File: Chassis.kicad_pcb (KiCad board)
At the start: 4 copper layers, 80 x 80.1 mm, 75 parts, among them IC1 LV2862YDDCR, IC2 RT6285GSP, J1 FR_JST, J10 IN_XT30, J11 SWD_IN, J12 Conn_01x08_Pin, J13 GIM1_JST, J14 GIM2_JST, J15 GIM1_XT30, J16 GIM2_XT30, J17 SWD_OUT, J18 CHA_XT30, J19 SHOO_XT30, J2 BR_JST, J20 GIM_XT30, J21 OUT_JST, J22 5V_XT30, J23 UART_IN, J24 UART_Out, J25 REF_IN, J26 REF_OUT, J27 CAN2_IN, J28 CAN2_OUT, J3 FL_JST, J4 BL_JST, J5 FR_XT30, J6 BR_XT30, J7 FL_XT30, J8 BL_XT30, J9 IN_JST

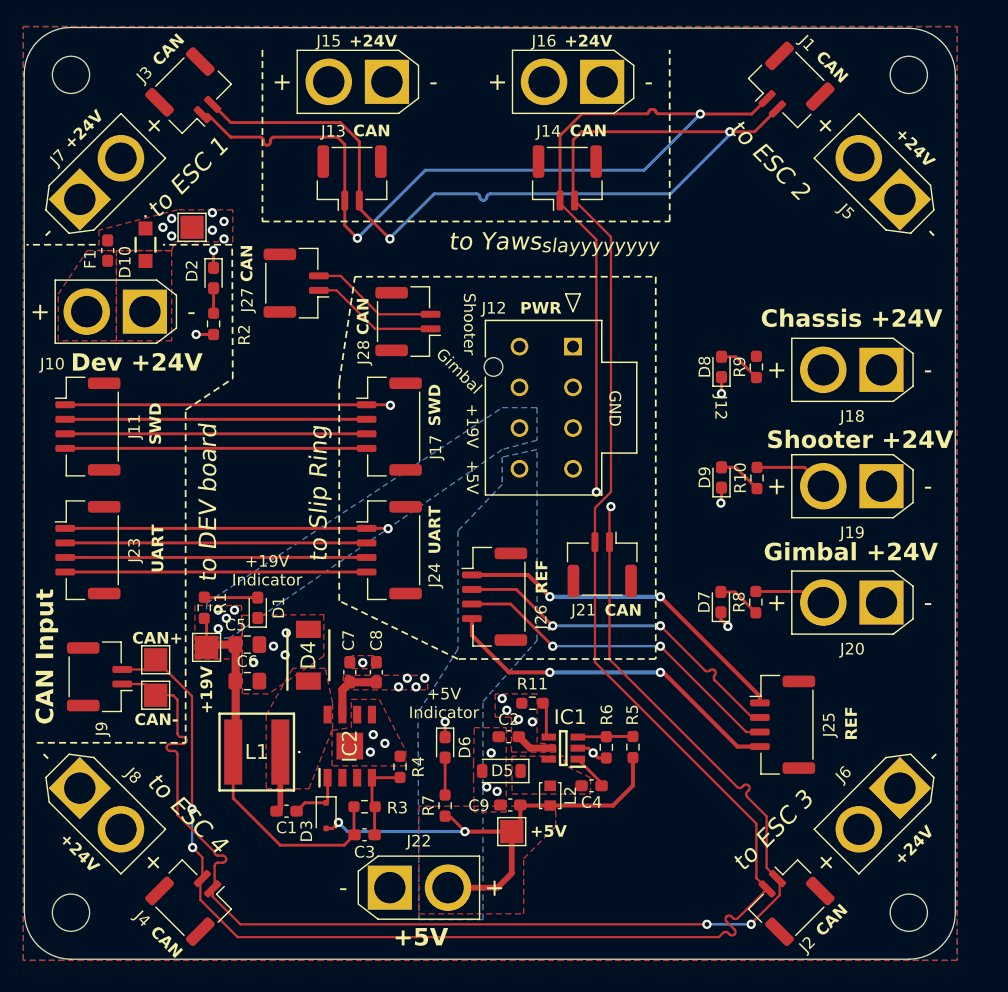
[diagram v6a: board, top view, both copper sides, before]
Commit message: Replace inductor with larger
Idk how much current it'll need + invalid inductor data for spreadsheet
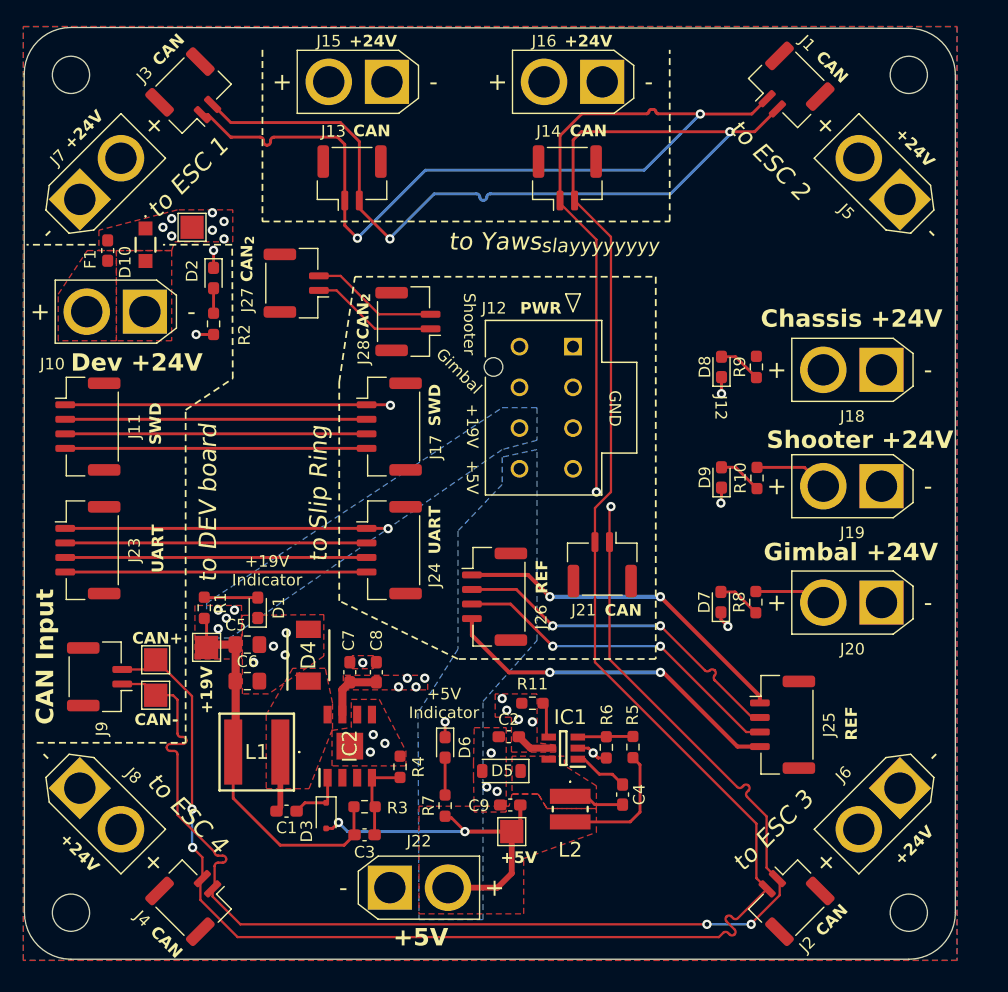
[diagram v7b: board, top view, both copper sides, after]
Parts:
- L2: footprint Inductor_SMD:L_Murata_LQH2MCNxxxx02_2.0x1.6mm -> Robomaster_Passives:SRN3012BTA330M
- moved C4 2.77 mm to (99.8, 91.2), turned to -90 degrees
- moved L2 2.07 mm to (95.2, 92.5)
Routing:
- net /24V -> 19V Buck Convertor/SW_{5}: track 0.00 -> 4.80 mm
- net /24V -> 19V Buck Convertor/BOOT_{5}: track 2.89 -> 4.75 mm
- net +5V: track 42.6 -> 41.1 mm
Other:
- board text added: "CAN_{2}"

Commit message: Update and generate IBOM
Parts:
- C2: value 2.2 μF -> 2.2μF
- C4: value 100 nF -> 100nF
- C9: value 10 nF -> 10nF
- F1: value Fuse -> 2.5A
- L2: value 33 μH -> 33μH
- R5: value 56 kΩ -> 56kΩ
- R6: value 10 kΩ -> 10kΩ
